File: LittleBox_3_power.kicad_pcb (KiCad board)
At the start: 2 copper layers, 200 x 90 mm, 113 parts, among them P10 CONN_01X03, P13 CONN_01X03, P16 CONN_01X03, P17 CONN_01X03, P18 CONN_01X01, P19 CONN_01X03, P20 CONN_01X01, P21 CONN_01X01, P23 CONN_01X02, P24 CONN_01X02, P25 CONN_01X02, P26 CONN_01X02, P27 CONN_01X02, P28 CONN_01X03, P29 CONN_01X02, P3 CONN_01X01, P30 CONN_01X03, P31 CONN_01X02, P32 CONN_01X03, P4 CONN_01X01, P400IN+1 CONN_1, P400IN-1 CONN_1, P9 CONN_01X03, Q1 C3M0065090D, Q10 IPW6045CP, Q2 C3M0065090D, Q3 C3M0065090D, Q4 C3M0065090D, Q5 C3M0065090D, Q6 C3M0065090D, Q7 IPW6045CP, Q8 IPW6045CP, Q9 IPW6045CP, U18 ACS712, U19 ACS712, U21 ACS712, U23 ACS712, U5 ACS712, U6 ACS712

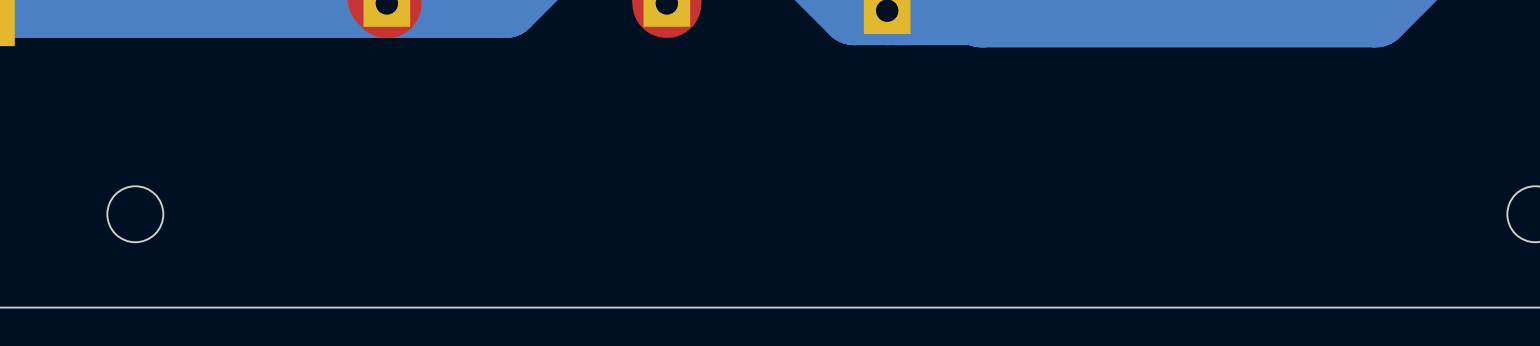
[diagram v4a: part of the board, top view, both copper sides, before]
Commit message: Correction masque incorrect sur C53 Ajout texte Suppression de git de fichiers inutiles
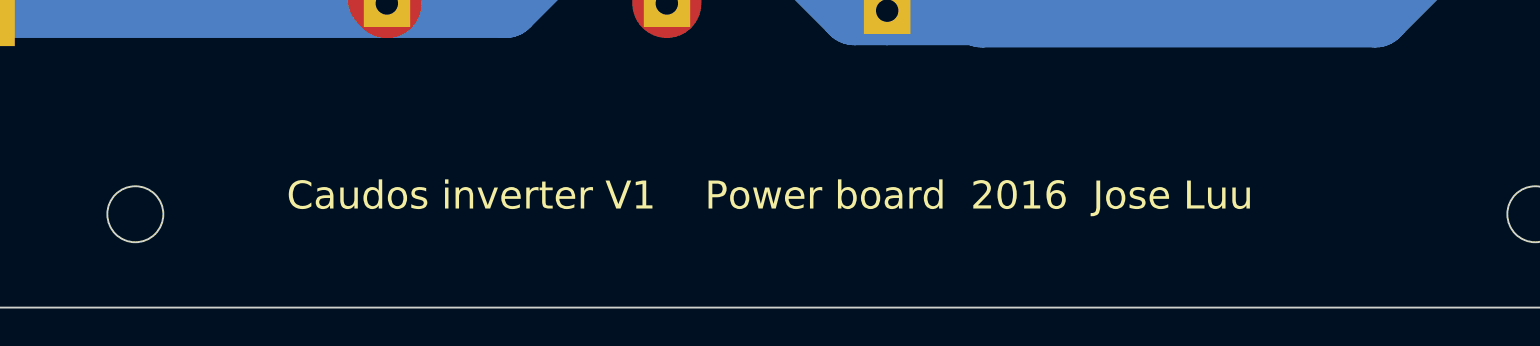
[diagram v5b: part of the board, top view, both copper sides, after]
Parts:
- removed the ? at (230.8, 66.4) (x2)
- added ? (x2): , inverter:hole_3mm, F.Cu at (230.8, 66.4)
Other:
- board text added: "Caudos inverter V1 Power board 2016 Jose Luu"
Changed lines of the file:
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@@
     (area 37.386904 29.616199 262.613096 140.050001)
     (thickness 1.6)
-    (drawings 39)
+    (drawings 40)
     (tracks 560)
     (zones 0)
@@
     (add_net "Net-(C33-Pad1)")
   )
+  (module inverter:MLCC_SuperCap_5750_BackCu (layer F.Cu)
+    (at 55.164 78.129)
+    (fp_text reference C48 (at 0 0.5) (layer F.SilkS)
+      (effects (font (size 1 1) (thickness 0.15)))
+    )
+    (fp_text value "2.2uF 630V" (at 0 -0.5) (layer F.Fab) hide
+      (effects (font (size 1 1) (thickness 0.15)))
+    )
+    (pad 1 smd rect (at -2.45 0) (size 2.1 5) (layers B.Cu B.Paste B.Mask)
+      (net 37 GND_12))
+    (pad 2 smd rect (at 2.45 0) (size 2.1 5) (layers B.Cu B.Paste B.Mask)
+      (net 31 "Net-(C48-Pad2)"))
+  )
+  (module inverter:MLCC_SuperCap_5750_BackCu (layer F.Cu)
+    (at 55.164 84.029)
+    (fp_text reference C51 (at 0 0.5) (layer F.SilkS)
+      (effects (font (size 1 1) (thickness 0.15)))
+    )
+    (fp_text value "1uF 630V" (at 0 -0.5) (layer F.Fab) hide
+      (effects (font (size 1 1) (thickness 0.15)))
+    )
+    (pad 1 smd rect (at -2.45 0) (size 2.1 5) (layers B.Cu B.Paste B.Mask)
+      (net 37 GND_12))
+    (pad 2 smd rect (at 2.45 0) (size 2.1 5) (layers B.Cu B.Paste B.Mask)
+      (net 31 "Net-(C48-Pad2)"))
+  )
+  (module inverter:MLCC_SuperCap_5750_BackCu (layer F.Cu)
+    (at 55.164 89.929)
+    (fp_text reference C52 (at 0 0.5) (layer F.SilkS)
+      (effects (font (size 1 1) (thickness 0.15)))
+    )
+    (fp_text value "1uF 630V" (at 0 -0.5) (layer F.Fab) hide
+      (effects (font (size 1 1) (thickness 0.15)))
+    )
+    (pad 1 smd rect (at -2.45 0) (size 2.1 5) (layers B.Cu B.Paste B.Mask)
+      (net 37 GND_12))
+    (pad 2 smd rect (at 2.45 0) (size 2.1 5) (layers B.Cu B.Paste B.Mask)
+      (net 31 "Net-(C48-Pad2)"))
+  )
+  (module inverter:MLCC_SuperCap_5750_BackCu (layer F.Cu)
+    (at 55.164 95.629)
+    (fp_text reference C53 (at 0 0.5) (layer F.SilkS)
+      (effects (font (size 1 1) (thickness 0.15)))
+    )
+    (fp_text value "1uF 630V" (at 0 -0.5) (layer F.Fab) hide
+      (effects (font (size 1 1) (thickness 0.15)))
+    )
+    (pad 1 smd rect (at -2.45 0) (size 2.1 5) (layers B.Cu B.Paste B.Mask)
+      (net 37 GND_12))
+    (pad 2 smd rect (at 2.45 0) (size 2.1 5) (layers B.Cu B.Paste B.Mask)
+      (net 31 "Net-(C48-Pad2)"))
+  )
   (module Resistors_SMD:R_1206_HandSoldering (layer F.Cu)
     (at 122.644 108.594 90)
@@
       (net 37 GND_12))
   )
-  (module inverter:MLCC_SuperCap_5750_BackCu (layer F.Cu)
-    (at 55.164 78.129)
-    (fp_text reference C48 (at 0 0.5) (layer F.SilkS)
-      (effects (font (size 1 1) (thickness 0.15)))
-    )
-    (fp_text value "2.2uF 630V" (at 0 -0.5) (layer F.Fab) hide
-      (effects (font (size 1 1) (thickness 0.15)))
-    )
-    (pad 1 smd rect (at -2.45 0) (size 2.1 5) (layers B.Cu F.Paste F.Mask)
-      (net 37 GND_12))
-    (pad 2 smd rect (at 2.45 0) (size 2.1 5) (layers B.Cu F.Paste F.Mask)
-      (net 31 "Net-(C48-Pad2)"))
-  )
-  (module inverter:MLCC_SuperCap_5750_BackCu (layer F.Cu)
-    (at 55.164 84.029)
-    (fp_text reference C51 (at 0 0.5) (layer F.SilkS)
-      (effects (font (size 1 1) (thickness 0.15)))
-    )
-    (fp_text value "1uF 630V" (at 0 -0.5) (layer F.Fab) hide
-      (effects (font (size 1 1) (thickness 0.15)))
-    )
-    (pad 1 smd rect (at -2.45 0) (size 2.1 5) (layers B.Cu F.Paste F.Mask)
-      (net 37 GND_12))
-    (pad 2 smd rect (at 2.45 0) (size 2.1 5) (layers B.Cu F.Paste F.Mask)
-      (net 31 "Net-(C48-Pad2)"))
-  )
-  (module inverter:MLCC_SuperCap_5750_BackCu (layer F.Cu)
-    (at 55.164 89.929)
-    (fp_text reference C52 (at 0 0.5) (layer F.SilkS)
-      (effects (font (size 1 1) (thickness 0.15)))
-    )
-    (fp_text value "1uF 630V" (at 0 -0.5) (layer F.Fab) hide
-      (effects (font (size 1 1) (thickness 0.15)))
-    )
-    (pad 1 smd rect (at -2.45 0) (size 2.1 5) (layers B.Cu F.Paste F.Mask)
-      (net 37 GND_12))
-    (pad 2 smd rect (at 2.45 0) (size 2.1 5) (layers B.Cu F.Paste F.Mask)
-      (net 31 "Net-(C48-Pad2)"))
-  )
-  (module inverter:MLCC_SuperCap_5750_BackCu (layer F.Cu)
-    (at 55.164 95.629)
-    (fp_text reference C53 (at 0 0.5) (layer F.SilkS)
-      (effects (font (size 1 1) (thickness 0.15)))
-    )
-    (fp_text value "1uF 630V" (at 0 -0.5) (layer F.Fab) hide
-      (effects (font (size 1 1) (thickness 0.15)))
-    )
-    (pad 1 smd rect (at -2.45 0) (size 2.1 5) (layers B.Cu F.Paste F.Mask)
-      (net 37 GND_12))
-    (pad 2 smd rect (at 2.45 0) (size 2.1 5) (layers B.Cu F.Paste F.Mask)
-      (net 31 "Net-(C48-Pad2)"))
-  )
   (module Fiducials:Fiducial_1mm_Dia_2.54mm_Outer_CopperTop (layer F.Cu)
     (at 55 135)
@@
       (solder_mask_margin 0.77) (clearance 0.77))
   )
+  (gr_text "Caudos inverter V1    Power board  2016  Jose Luu" (at 109 134) (layer F.SilkS)
+    (effects (font (size 1.5 1.5) (thickness 0.3)))
+  )
   (gr_circle (center 150 135) (end 150 136.5) (layer Edge.Cuts) (width 0.1))

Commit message: Indications dans Cmts.User
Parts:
- removed ? (x15): , inverter:hole_3mm
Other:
- board text added: "<- Hole 3mm diameter"
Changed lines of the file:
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@@
     (area 37.386904 29.616199 262.613096 140.050001)
     (thickness 1.6)
-    (drawings 40)
+    (drawings 41)
     (tracks 560)
     (zones 0)
-    (modules 113)
+    (modules 98)
     (nets 61)
   )
@@
     (33 F.Adhes user hide)
     (34 B.Paste user hide)
-    (35 F.Paste user hide)
+    (35 F.Paste user)
     (36 B.SilkS user)
-    (37 F.SilkS user)
-    (38 B.Mask user hide)
-    (39 F.Mask user hide)
+    (37 F.SilkS user hide)
+    (38 B.Mask user)
+    (39 F.Mask user)
     (40 Dwgs.User user hide)
-    (41 Cmts.User user hide)
+    (41 Cmts.User user)
     (42 Eco1.User user hide)
     (43 Eco2.User user hide)
@@
     (pad_to_mask_clearance 0)
     (pad_to_paste_clearance -0.07)
-    (aux_axis_origin 55 135)
-    (grid_origin 55 135)
-    (visible_elements 7FFFFF7F)
+    (aux_axis_origin 50 140)
+    (grid_origin 50 140)
+    (visible_elements 7FFFD77B)
     (pcbplotparams
-      (layerselection 0x010f0_80000001)
+      (layerselection 0x012f8_80000001)
       (usegerberextensions false)
       (excludeedgelayer true)
@@
       (net 26 "Net-(Q7-Pad2)"))
   )
-  (module inverter:hole_3mm (layer F.Cu)
-    (at 100.048 110.7128)
-    (fp_text reference "" (at 0 0) (layer F.SilkS)
-      (effects (font (thickness 0.15)))
-    )
-    (fp_text value "" (at 0 0) (layer F.SilkS)
-      (effects (font (thickness 0.15)))
-    )
-    (fp_circle (center 0 0) (end 1.5 0) (layer Dwgs.User) (width 0.05))
-    (pad "" np_thru_hole circle (at 0 0) (size 1.524 1.524) (drill 0.762) (layers Dwgs.User))
-  )
-  (module inverter:hole_3mm (layer F.Cu)
-    (at 84.048 61.3128)
-    (fp_text reference "" (at 0 0) (layer F.SilkS)
-      (effects (font (thickness 0.15)))
-    )
-    (fp_text value "" (at 0 0) (layer F.SilkS)
-      (effects (font (thickness 0.15)))
-    )
-    (fp_circle (center 0 0) (end 1.5 0) (layer Dwgs.User) (width 0.05))
-    (pad "" np_thru_hole circle (at 0 0) (size 1.524 1.524) (drill 0.762) (layers Dwgs.User))
-  )
-  (module inverter:hole_3mm (layer F.Cu)
-    (at 130.748 118.3128)
-    (fp_text reference "" (at 0 0) (layer F.SilkS)
-      (effects (font (thickness 0.15)))
-    )
-    (fp_text value "" (at 0 0) (layer F.SilkS)
-      (effects (font (thickness 0.15)))
-    )
-    (fp_circle (center 0 0) (end 1.5 0) (layer Dwgs.User) (width 0.05))
-    (pad "" np_thru_hole circle (at 0 0) (size 1.524 1.524) (drill 0.762) (layers Dwgs.User))
-  )
-  (module inverter:hole_3mm (layer F.Cu)
-    (at 130.748 67.9128)
-    (fp_text reference "" (at 0 0) (layer F.SilkS)
-      (effects (font (thickness 0.15)))
-    )
-    (fp_text value "" (at 0 0) (layer F.SilkS)
-      (effects (font (thickness 0.15)))
-    )
-    (fp_circle (center 0 0) (end 1.5 0) (layer Dwgs.User) (width 0.05))
-    (pad "" np_thru_hole circle (at 0 0) (size 1.524 1.524) (drill 0.762) (layers Dwgs.User))
-  )
-  (module inverter:hole_3mm (layer F.Cu)
-    (at 160.448 118.3128)
-    (fp_text reference "" (at 0 0) (layer F.SilkS)
-      (effects (font (thickness 0.15)))
-    )
-    (fp_text value "" (at 0 0) (layer F.SilkS)
-      (effects (font (thickness 0.15)))
-    )
-    (fp_circle (center 0 0) (end 1.5 0) (layer Dwgs.User) (width 0.05))
-    (pad "" np_thru_hole circle (at 0 0) (size 1.524 1.524) (drill 0.762) (layers Dwgs.User))
-  )
-  (module inverter:hole_3mm (layer F.Cu)
-    (at 160.448 68.7128)
-    (fp_text reference "" (at 0 0) (layer F.SilkS)
-      (effects (font (thickness 0.15)))
-    )
-    (fp_text value "" (at 0 0) (layer F.SilkS)
-      (effects (font (thickness 0.15)))
-    )
-    (fp_circle (center 0 0) (end 1.5 0) (layer Dwgs.User) (width 0.05))
-    (pad "" np_thru_hole circle (at 0 0) (size 1.524 1.524) (drill 0.762) (layers Dwgs.User))
-  )
-  (module inverter:hole_3mm (layer F.Cu)
-    (at 213.048 66.4128)
-    (fp_text reference "" (at 0 0) (layer F.SilkS)
-      (effects (font (thickness 0.15)))
-    )
-    (fp_text value "" (at 0 0) (layer F.SilkS)
-      (effects (font (thickness 0.15)))
-    )
-    (fp_circle (center 0 0) (end 1.5 0) (layer Dwgs.User) (width 0.05))
-    (pad "" np_thru_hole circle (at 0 0) (size 1.524 1.524) (drill 0.762) (layers Dwgs.User))
-  )
-  (module inverter:hole_3mm (layer F.Cu)
-    (at 213.048 116.8128)
-    (fp_text reference "" (at 0 0) (layer F.SilkS)
-      (effects (font (thickness 0.15)))
-    )
-    (fp_text value "" (at 0 0) (layer F.SilkS)
-      (effects (font (thickness 0.15)))
-    )
-    (fp_circle (center 0 0) (end 1.5 0) (layer Dwgs.User) (width 0.05))
-    (pad "" np_thru_hole circle (at 0 0) (size 1.524 1.524) (drill 0.762) (layers Dwgs.User))
-  )
-  (module inverter:hole_3mm (layer F.Cu)
-    (at 230.848 66.4128)
-    (fp_text reference "" (at 0 0) (layer F.SilkS)
-      (effects (font (thickness 0.15)))
-    )
-    (fp_text value "" (at 0 0) (layer F.SilkS)
-      (effects (font (thickness 0.15)))
-    )
-    (fp_circle (center 0 0) (end 1.5 0) (layer Dwgs.User) (width 0.05))
-    (pad "" np_thru_hole circle (at 0 0) (size 1.524 1.524) (drill 0.762) (layers Dwgs.User))
-  )
-  (module inverter:hole_3mm (layer F.Cu)
-    (at 230.848 66.4128)
-    (fp_text reference "" (at 0 0) (layer F.SilkS)
-      (effects (font (thickness 0.15)))
-    )
-    (fp_text value "" (at 0 0) (layer F.SilkS)
-      (effects (font (thickness 0.15)))
-    )
-    (fp_circle (center 0 0) (end 1.5 0) (layer Dwgs.User) (width 0.05))
-    (pad "" np_thru_hole circle (at 0 0) (size 1.524 1.524) (drill 0.762) (layers Dwgs.User))
-  )
-  (module inverter:hole_3mm (layer F.Cu)
-    (at 230.848 116.8128)
-    (fp_text reference "" (at 0 0) (layer F.SilkS)
-      (effects (font (thickness 0.15)))
-    )
-    (fp_text value "" (at 0 0) (layer F.SilkS)
-      (effects (font (thickness 0.15)))
-    )
-    (fp_circle (center 0 0) (end 1.5 0) (layer Dwgs.User) (width 0.05))
-    (pad "" np_thru_hole circle (at 0 0) (size 1.524 1.524) (drill 0.762) (layers Dwgs.User))
-  )
-  (module inverter:hole_3mm (layer F.Cu)
-    (at 85.048 106.4128)
-    (fp_text reference "" (at 0 0) (layer F.SilkS)
-      (effects (font (thickness 0.15)))
-    )
-    (fp_text value "" (at 0 0) (layer F.SilkS)
-      (effects (font (thickness 0.15)))
-    )
-    (fp_circle (center 0 0) (end 1.5 0) (layer Dwgs.User) (width 0.05))
-    (pad "" np_thru_hole circle (at 0 0) (size 1.524 1.524) (drill 0.762) (layers Dwgs.User))
-  )
-  (module inverter:hole_3mm (layer F.Cu)
-    (at 102.348 65.5128)
-    (fp_text reference "" (at 0 0) (layer F.SilkS)
-      (effects (font (thickness 0.15)))
-    )
-    (fp_text value "" (at 0 0) (layer F.SilkS)
-      (effects (font (thickness 0.15)))
-    )
-    (fp_circle (center 0 0) (end 1.5 0) (layer Dwgs.User) (width 0.05))
-    (pad "" np_thru_hole circle (at 0 0) (size 1.524 1.524) (drill 0.762) (layers Dwgs.User))
-  )
-  (module inverter:hole_3mm (layer F.Cu)
-    (at 146.048 113.5128)
-    (fp_text reference "" (at 0 0) (layer F.SilkS)
-      (effects (font (thickness 0.15)))
-    )
-    (fp_text value "" (at 0 0) (layer F.SilkS)
-      (effects (font (thickness 0.15)))
-    )
-    (fp_circle (center 0 0) (end 1.5 0) (layer Dwgs.User) (width 0.05))
-    (pad "" np_thru_hole circle (at 0 0) (size 1.524 1.524) (drill 0.762) (layers Dwgs.User))
-  )
-  (module inverter:hole_3mm (layer F.Cu)
-    (at 146.048 72.4128)
-    (fp_text reference "" (at 0 0) (layer F.SilkS)
-      (effects (font (thickness 0.15)))
-    )
-    (fp_text value "" (at 0 0) (layer F.SilkS)
-      (effects (font (thickness 0.15)))
-    )
-    (fp_circle (center 0 0) (end 1.5 0) (layer Dwgs.User) (width 0.05))
-    (pad "" np_thru_hole circle (at 0 0) (size 1.524 1.524) (drill 0.762) (layers Dwgs.User))
-  )
   (module Resistors_SMD:R_1206_HandSoldering (layer F.Cu)
     (at 95.974 66.684 90)
@@
       (solder_mask_margin 0.77) (clearance 0.77))
   )
-  (gr_text "Caudos inverter V1    Power board  2016  Jose Luu" (at 109 134) (layer F.SilkS)
+  (gr_text "<- Hole 3mm diameter" (at 91 135) (layer Cmts.User)
     (effects (font (size 1.5 1.5) (thickness 0.3)))
   )
+  (gr_text "Caudos inverter V1    Power board  2016  Jose Luu" (at 111 135) (layer F.SilkS)
+    (effects (font (size 1.5 1.5) (thickness 0.3)))
+  )
